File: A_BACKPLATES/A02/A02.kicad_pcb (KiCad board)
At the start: 2 copper layers, 183 x 110 mm, 203 parts, among them J0 Conn_01x01_Male, J1 Conn_01x01_Male, J2 Conn_01x01_Male, J3 Conn_01x01_Male

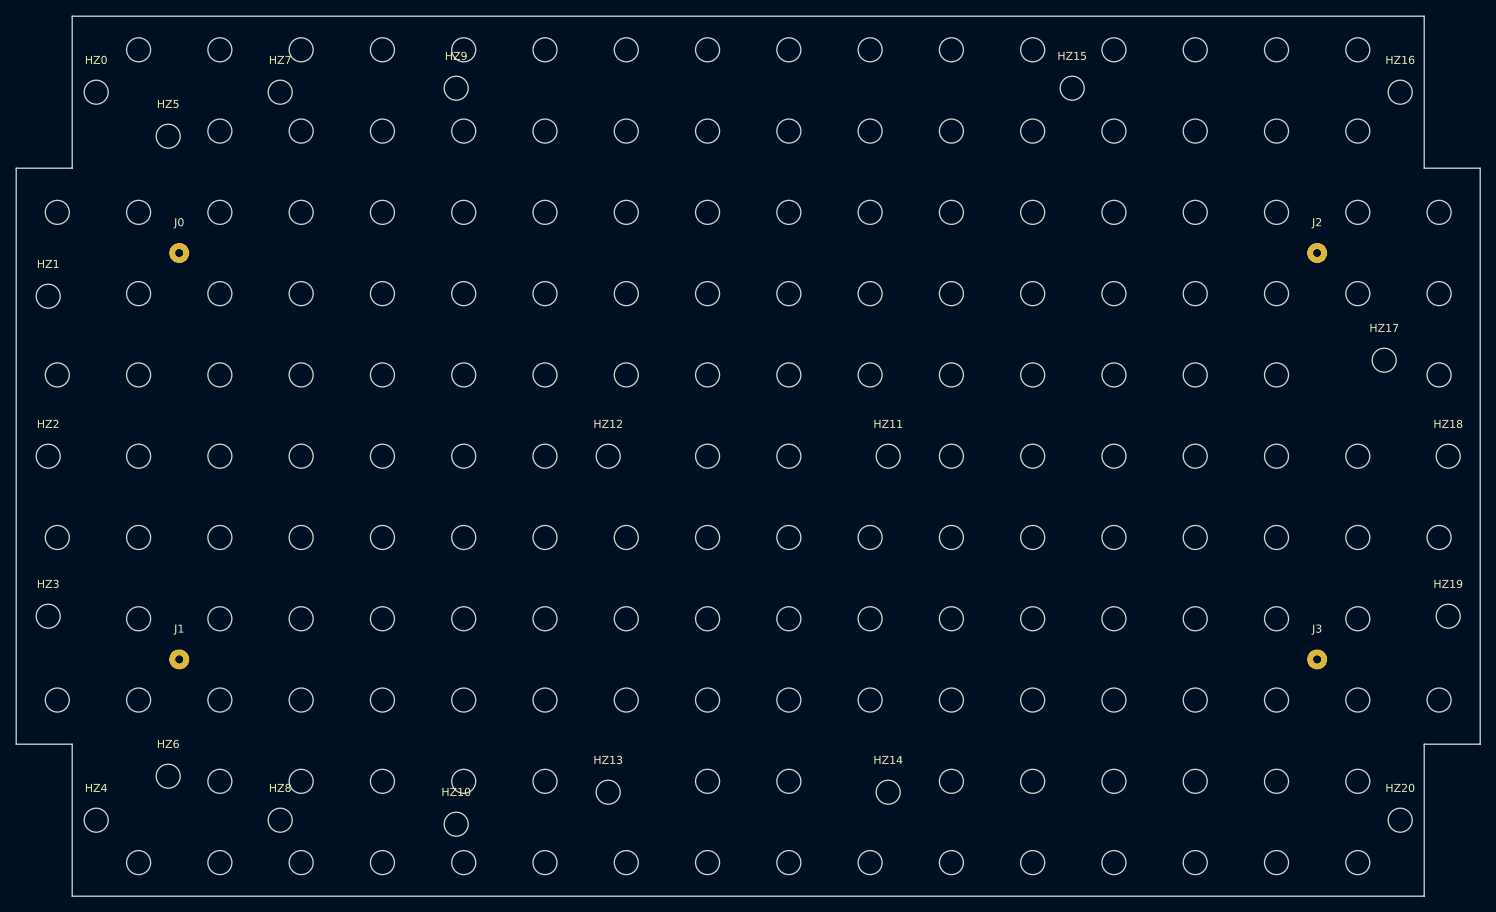
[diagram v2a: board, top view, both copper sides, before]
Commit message: fixed some misplaced enclosure holes
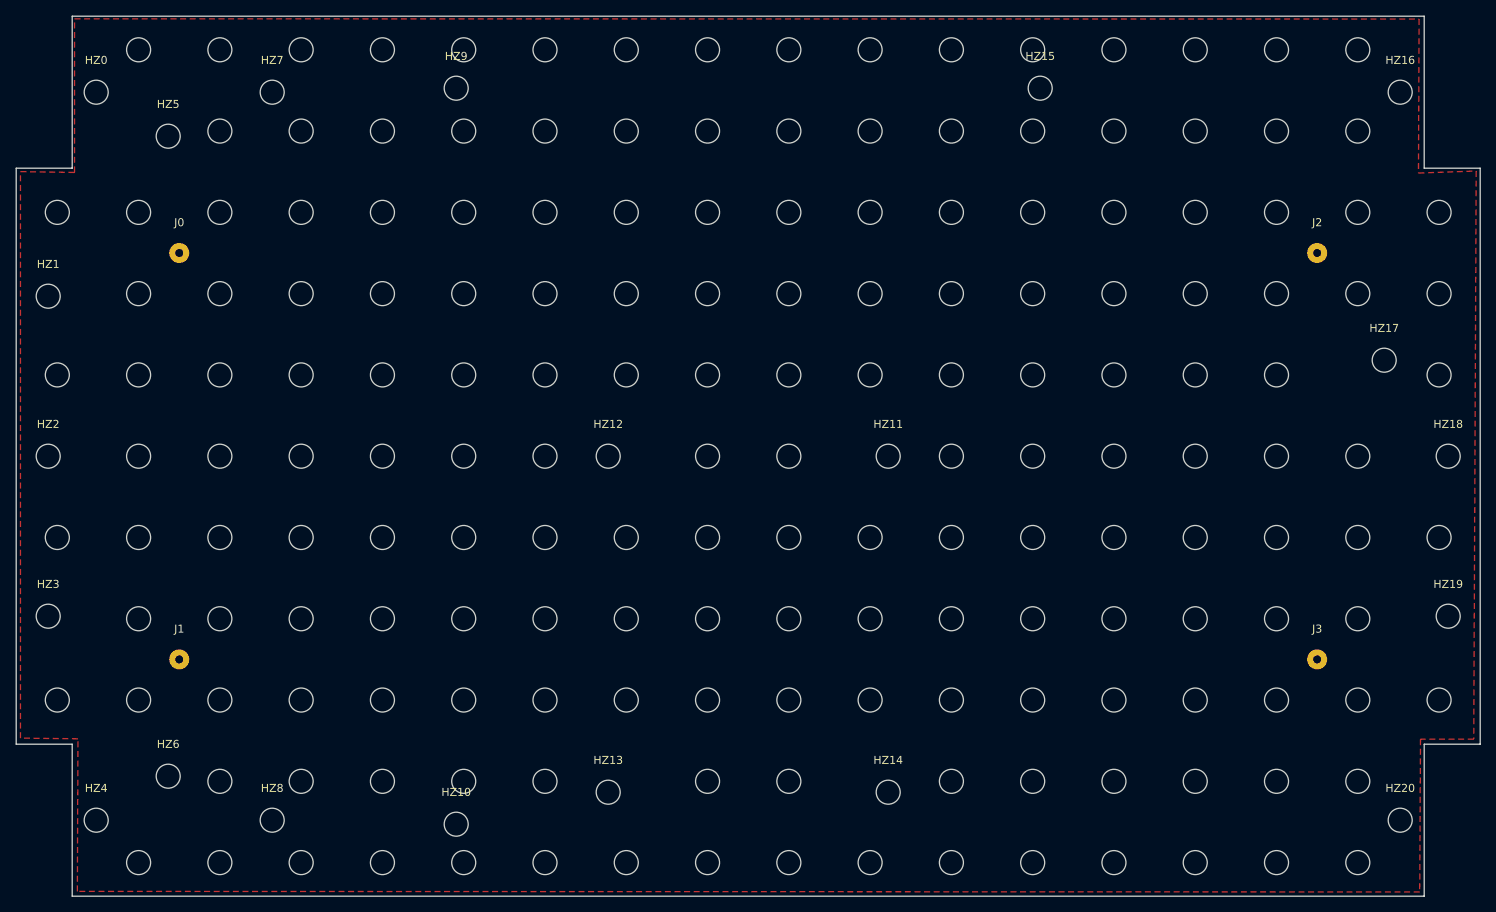
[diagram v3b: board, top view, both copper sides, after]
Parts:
- moved HZ15 4.00 mm to (146.7, 28.6)
- moved HZ7 1.00 mm to (50.7, 29.1)
- moved HZ8 1.00 mm to (50.7, 120.1)
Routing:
- added copper zone on F.Cu, net Net-(J0-Pad1)
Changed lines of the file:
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@@
   )
   (module MountingHole:MountingHole_3mm (layer F.Cu)
-    (at 150.67 28.61)
+    (at 146.67 28.61)
     (descr "Mounting Hole 3mm, no annular")
     (tags "mounting hole 3mm no annular")
@@
   )
   (module MountingHole:MountingHole_3mm (layer F.Cu)
-    (at 51.67 120.11)
+    (at 50.67 120.11)
     (descr "Mounting Hole 3mm, no annular")
     (tags "mounting hole 3mm no annular")
@@
   )
   (module MountingHole:MountingHole_3mm (layer F.Cu)
-    (at 51.67 29.11)
+    (at 50.67 29.11)
     (descr "Mounting Hole 3mm, no annular")
     (tags "mounting hole 3mm no annular")
@@
   (gr_line (start 25.67 19.61) (end 194.67 19.61) (layer Edge.Cuts) (width 0.05))
   (gr_line (start 18.67 38.61) (end 18.67 110.61) (layer Edge.Cuts) (width 0.05))
+  (zone (net 1) (net_name "Net-(J0-Pad1)") (layer F.Cu) (hatch edge 0.508)
+    (connect_pads (clearance 0.508))
+    (min_thickness 0.254)
+    (fill yes (arc_segments 32) (thermal_gap 0.508) (thermal_bridge_width 0.508))
+    (polygon
+      (pts
+        (xy 193.9544 39.2176) (xy 201.168 38.9636) (xy 200.8632 109.982) (xy 194.2084 109.982) (xy 194.1068 129.0828)
+        (xy 26.3144 129.0066) (xy 26.3906 109.9312) (xy 19.2024 109.855) (xy 19.2024 39.0398) (xy 25.9588 39.1414)
+        (xy 25.9588 19.939) (xy 194.0306 19.9644)
+      )
+    )
+  )
 )
